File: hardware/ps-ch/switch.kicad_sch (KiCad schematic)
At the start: 18 parts, among them Q4 PSMN059-150Y, Q9 PSMN059-150Y, U16 LM74502H, U18 74LVC126A, U20 74LVC126A

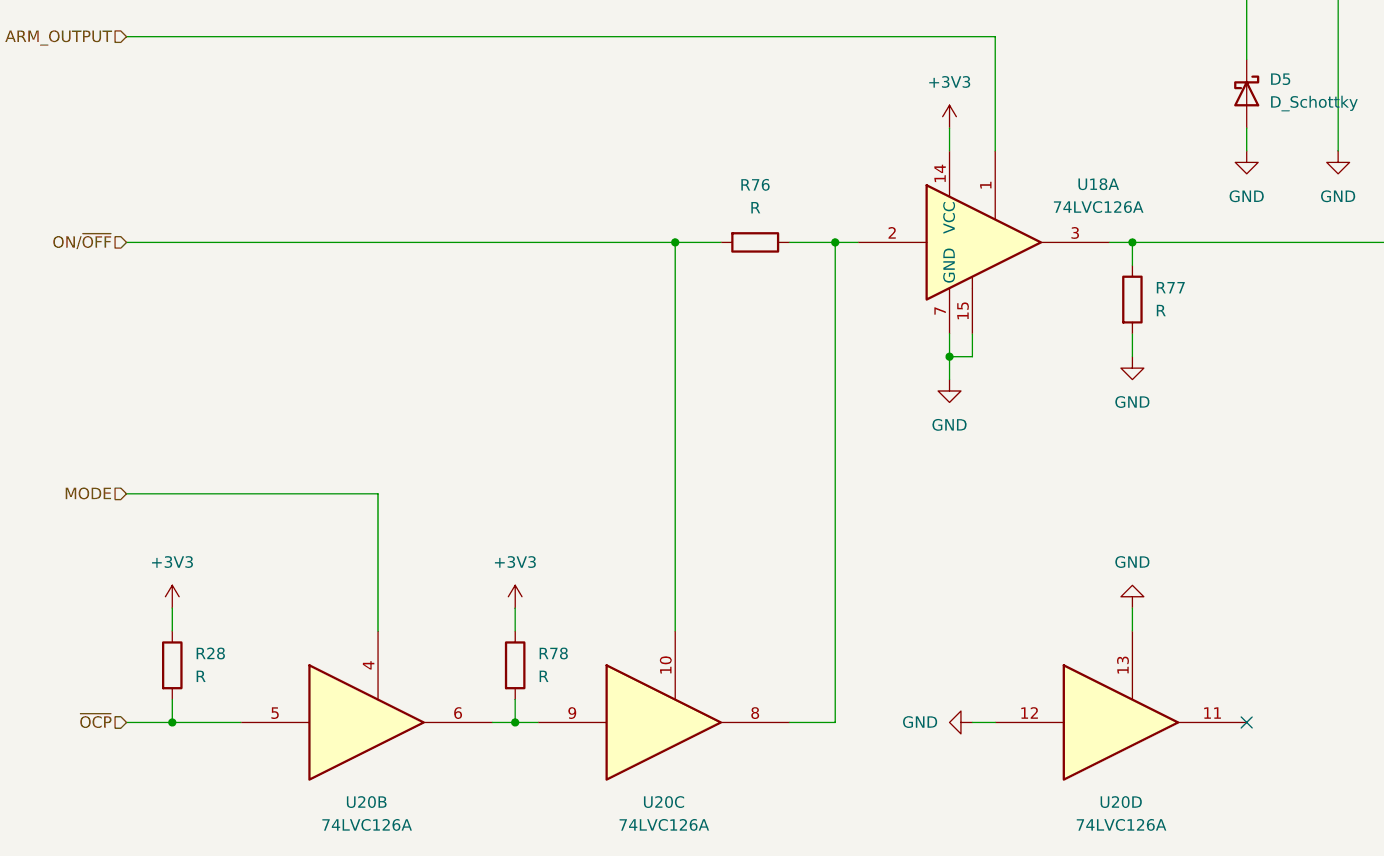
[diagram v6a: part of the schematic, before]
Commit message: - added component values/part numbers
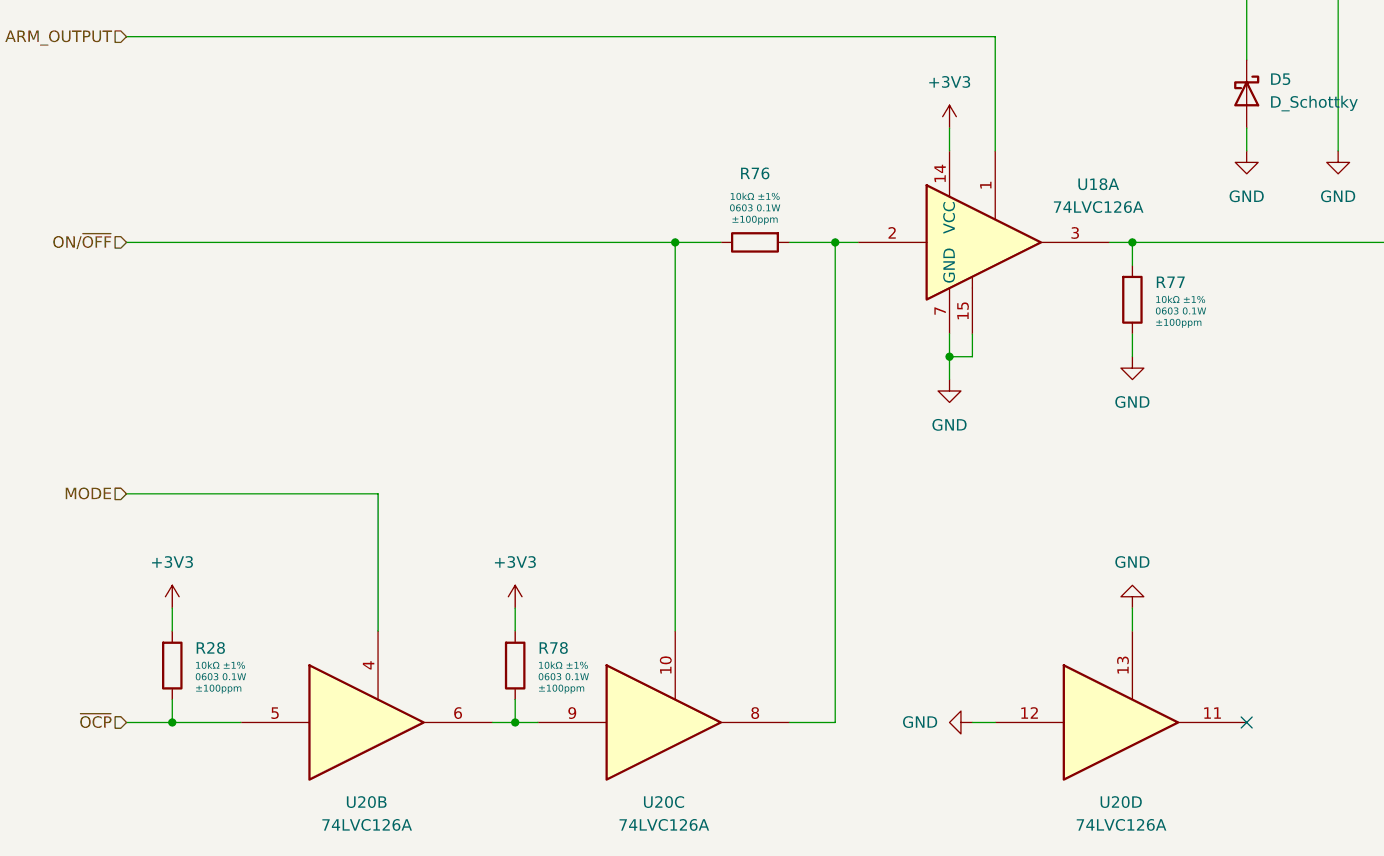
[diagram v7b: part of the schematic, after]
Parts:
- R28, R76, R77, R78: value R -> 10kΩ 0603 0.1W ±1% ±100ppm/°C; footprint (none) -> Resistor_SMD:R_0603_1608Metric; symbol Device:R -> ps-ch:10kΩ 0603 0.1W ±1% ±100ppm/°C; DisplayValue0 (none) -> 10kΩ ±1%; DisplayValue1 (none) -> 0603 0.1W; DisplayValue2 (none) -> ±100ppm; Manufacturer (none) -> Yageo; Manufacturer Part Number (none) -> AC0603FR-0710KL
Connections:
- net +3V3: now also R28.2, R78.2; no longer R28.1, R78.1
- net GND: now also R77.1; no longer R77.2
- net ON/~{OFF}: now also R76.1; no longer R76.2
- net ~{OCP}: now also R28.1; no longer R28.2
- net at U16.1 (EN/UVLO), U18.3: now also R77.2; no longer R77.1
- net at U20.6, U20.9: now also R78.1; no longer R78.2
- net at U18.2, U20.8: now also R76.2; no longer R76.1

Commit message: changed voltage regulation (preregulator)
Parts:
- removed C78: C, symbol Device:C
- removed D4, D5: D_Schottky, symbol Device:D_Schottky
- removed R74: R, symbol Device:R
- added C76: 0.1μF 0603 100Vdc X7R ±20%, Capacitor_SMD:C_0603_1608Metric, symbol ps-ch:0.1μF 0603 100Vdc X7R ±20%
- added D1, D4: PMEG60T30ELR, Diode_SMD:Nexperia_CFP3_SOD-123W, symbol ps-ch:PMEG60T30ELR
- added L15: 60Ω@100MHz, Inductor_SMD:L_0603_1608Metric, symbol ps-ch:74437349015
- C77: value C -> 0.22μF 0603 50Vdc X7R ±20%; footprint (none) -> Capacitor_SMD:C_0603_1608Metric; symbol Device:C -> ps-ch:0.22μF 0603 50Vdc X7R ±20%; DisplayValue0 (none) -> 0.22μF ±20%; DisplayValue1 (none) -> 0603 50Vdc; DisplayValue2 (none) -> X7R; Manufacturer (none) -> Murata; Manufacturer Part Number (none) -> GRM188R71H224MAC4
- C79: value C -> 1nF 0603 100Vdc X7R ±20%; footprint (none) -> Capacitor_SMD:C_0603_1608Metric; symbol Device:C -> ps-ch:1nF 0603 100Vdc X7R ±20%; DisplayValue0 (none) -> 1nF ±20%; DisplayValue1 (none) -> 0603 100Vdc; DisplayValue2 (none) -> X7R; Manufacturer (none) -> Murata; Manufacturer Part Number (none) -> GCD188R72A102MA01
- C80: value C -> 0.1μF 0603 100Vdc X7R ±20%; footprint (none) -> Capacitor_SMD:C_0603_1608Metric; symbol Device:C -> ps-ch:0.1μF 0603 100Vdc X7R ±20%; DisplayValue0 (none) -> 0.1μF ±20%; DisplayValue1 (none) -> 0603 100Vdc; DisplayValue2 (none) -> X7R; Manufacturer (none) -> Murata; Manufacturer Part Number (none) -> GRM188R72A104MA35
- R72: value R -> 0Ω 0603 0.1W ±1% ±100ppm/°C; footprint (none) -> Resistor_SMD:R_0603_1608Metric; symbol Device:R -> ps-ch:0Ω 0603 0.1W ±1% ±100ppm/°C; DisplayValue0 (none) -> 0Ω ±1%; DisplayValue1 (none) -> 0603 0.13W; DisplayValue2 (none) -> ±100ppm; Manufacturer (none) -> Yageo; Manufacturer Part Number (none) -> AC0603FR-070RL
- R73: value R -> 10kΩ 0603 0.1W ±1% ±100ppm/°C; footprint (none) -> Resistor_SMD:R_0603_1608Metric; symbol Device:R -> ps-ch:10kΩ 0603 0.1W ±1% ±100ppm/°C; DisplayValue0 (none) -> 10kΩ ±1%; DisplayValue1 (none) -> 0603 0.1W; DisplayValue2 (none) -> ±100ppm; Manufacturer (none) -> Yageo; Manufacturer Part Number (none) -> AC0603FR-0710KL; now not fitted
- R76: value 10kΩ 0603 0.1W ±1% ±100ppm/°C -> 1kΩ 0603 0.1W ±1% ±100ppm/°C; symbol ps-ch:10kΩ 0603 0.1W ±1% ±100ppm/°C -> ps-ch:1kΩ 0603 0.1W ±1% ±100ppm/°C; DisplayValue0 10kΩ ±1% -> 1kΩ ±1%; Manufacturer Part Number AC0603FR-0710KL -> AC0603FR-071KL
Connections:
- net GND: now also C79.1, C80.1, R72.2, C76.1, D1.2 (A), D4.2 (A); no longer C79.2, C80.2, R72.1
- net IN: now also C80.2, D1.1 (K); no longer C80.1
- net OUT: now also C79.2, R73.1, D4.1 (K); no longer C79.1, R73.2
- net VDC: now also L15.1
- net at C77.2: now also U16.5 (VS), C76.2, L15.2; no longer U16.4 (VCAP)
- net at C77.1: now also U16.4 (VCAP); no longer U16.5 (VS)
- new net: R72.1, R73.2, U16.7 (OV)
